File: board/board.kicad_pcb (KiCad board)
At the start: 2 copper layers, 91.3 x 53.3 mm, 87 parts, among them J1 USB_B_Micro, J4 SWD_CONN, J5 JTAG_CONN, J6 UART_Conn, J7 SPI_CONN, J8 I2C_CONN, SW1 SW_DP3T, SW2 SW_DP3T, SW3 SW_DPDT_x2, U1 FT2232H-56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

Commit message: Update for release.
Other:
- board text added: "Mode"
- board text added: "Rev 5 OSHW - Apache 2 (C) 2020 Google LLC Designed by @Matir"
- board text added: "Test Interface for Multiple Embedded Protocols (TIMEP)"
- board text removed: "Universal IoT Tool (UNIT) (C) 2019 Google LLC Designed by: David Tomaschik (@Matir) Rev 3"

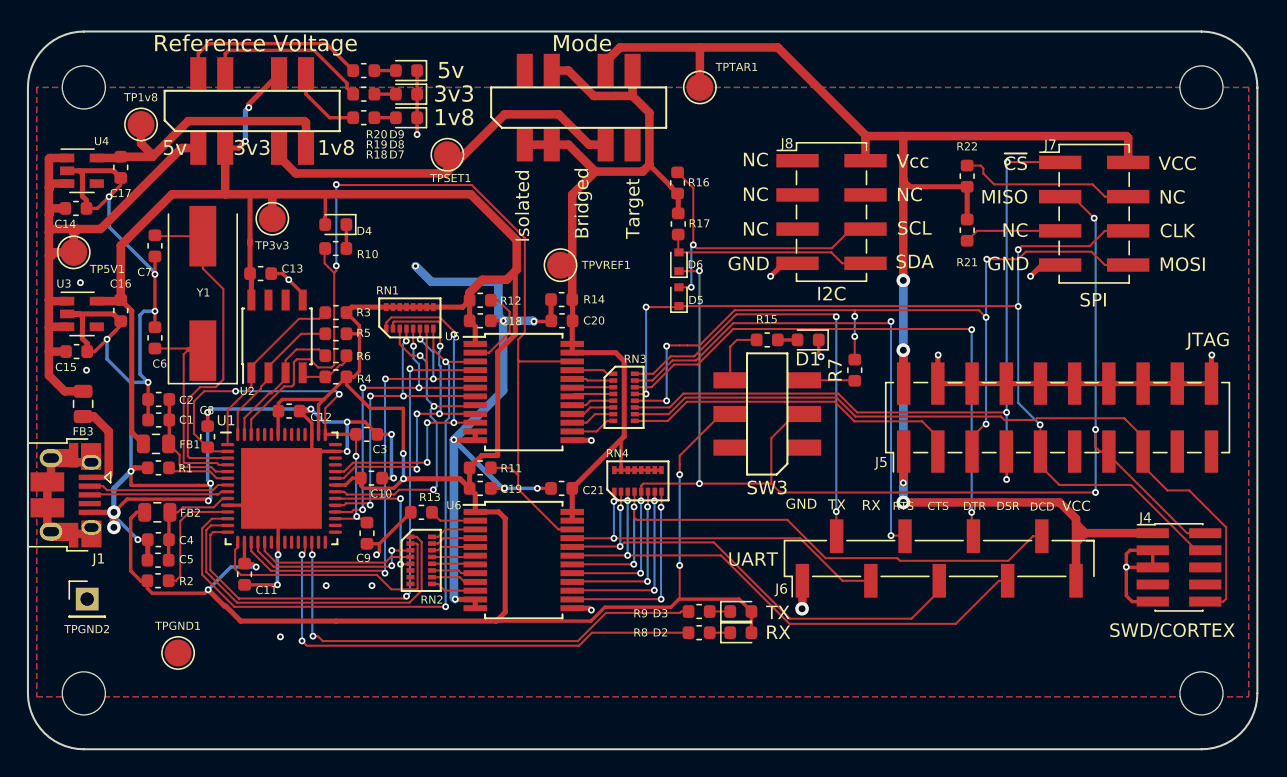
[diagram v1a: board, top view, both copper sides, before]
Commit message: Add protection (ESD, PTC fusing) to MicroUSB port
Schematic changes:

* No connect SHIELD on the MicroUSB port. Since we have no SHIELD GND, I
think it's best to leave the shield unconnected rather than connect it
to our digital GND and potentially introduce noise. This seems to be
backed up by the FTDI USB Design Guidelines
(https://www.ftdichip.com/Support/Documents/AppNotes/AN_146_USB_Hardware_Design_Guidelines_for_FTDI_ICs.pdf)
* Inline a USBLC-6 for transient voltage supression on our USB data lines
and VBUS
* Add a 500mA hold current PTC after the ferrite bead on VBUS. This PTC
should help protect the host computer if the board short circuits

Layout changes:

* Moves the passives (C2, C1, FB1, R1, FB2, C4, C5, R2) around the
MicroUSB port slightly outward to make room for the USBLC-6
* Place USBLC-6 close to the MicroUSB port
* Place PTC next to FB3

Component Selection:

* USBLC-6 is a popular choice for USB transient voltage supression. It's
very low capacitance so it shouldn't have an impact on data
integrity/speed. The SOT-666 package is common and compact, but still
easy enough to place by hand. It's also cheap at just $0.32 (100x)
* The Littelfuse NanoSMD fuse is rated for 13.2V and a 500mA hold
current. It trips at 1.1A with a fast 100ms time to trip. The 1206
footprint is compact and it's easy to place by hand. It's pretty cheap
at $0.32 (100x)
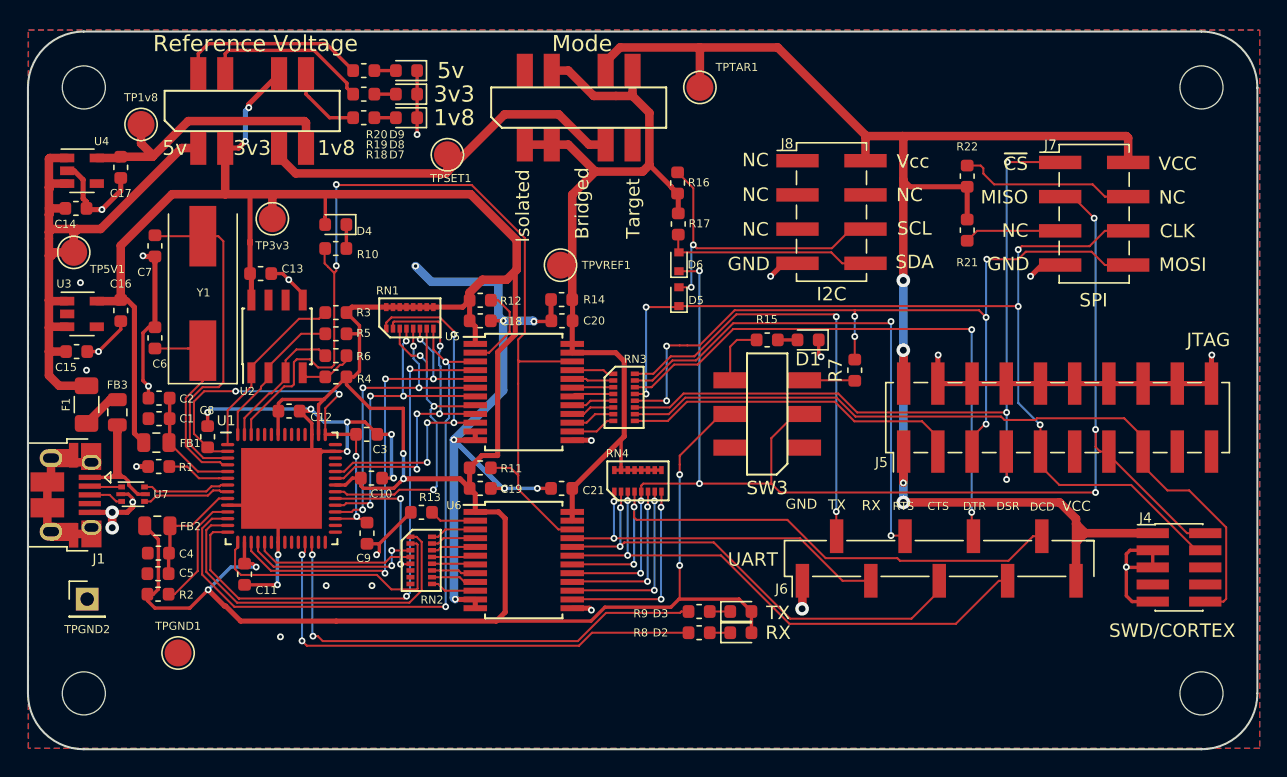
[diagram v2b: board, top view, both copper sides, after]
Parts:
- added F1: 500mA, Fuse:Fuse_1206_3216Metric, F.Cu at (92.2, 106.6)
- added U7: USBLC6, Package_TO_SOT_SMD:SOT-666, F.Cu at (95.7, 113.2)
- moved FB3 2.61 mm to (94.5, 107.1)
- moved C4 1.00 mm to (97.5, 117.6)
- moved C5 1.00 mm to (97.5, 119.1)
- moved FB2 1.00 mm to (97.5, 115.6)
- moved R2 1.00 mm to (97.5, 120.6)
- moved C1 0.10 mm to (97.6, 107.6)
- moved C2 0.10 mm to (97.6, 106.1)
- moved FB1 0.10 mm to (97.4, 109.4)
- moved R1 0.10 mm to (97.6, 111.2)
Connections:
- net Net-(FB3-Pad2) renamed /VBUS
- FB3 pad 1: +5V -> Net-(F1-Pad2)
- J1 pad 2: /USB_N -> Net-(J1-Pad2)
- J1 pad 3: /USB_P -> Net-(J1-Pad3)
- J1 pad 4: Net-(J1-Pad4) -> (no net)
- J1 pad 6: GND -> Net-(J1-Pad6)
- J4 pad 6: Net-(J4-Pad6) -> (no net)
- J4 pad 7: Net-(J4-Pad7) -> (no net)
- J4 pad 8: Net-(J4-Pad8) -> (no net)
- J5 pad 11: Net-(J5-Pad11) -> (no net)
- J5 pad 17: Net-(J5-Pad17) -> (no net)
- J5 pad 19: Net-(J5-Pad19) -> (no net)
- J8 pad 1: Net-(J8-Pad1) -> (no net)
- J8 pad 3: Net-(J8-Pad3) -> (no net)
- J8 pad 4: Net-(J8-Pad4) -> (no net)
- J8 pad 5: Net-(J8-Pad5) -> (no net)
- RN2 pad 6: Net-(RN2-Pad6) -> (no net)
- RN2 pad 7: Net-(RN2-Pad7) -> (no net)
- RN2 pad 8: Net-(RN2-Pad8) -> (no net)
- SW2 pad 4: Net-(SW2-Pad4) -> (no net)
- SW2 pad 5: Net-(SW2-Pad5) -> (no net)
- SW3 pad 1: Net-(SW3-Pad1) -> (no net)
- SW3 pad 4: Net-(SW3-Pad4) -> (no net)
- U1 pad 20: /FT2232 Module/ADBUS7 -> (no net)
- U1 pad 22: /FT2232 Module/ACBUS0 -> (no net)
- U1 pad 23: /FT2232 Module/ACBUS1 -> (no net)
- U1 pad 24: /FT2232 Module/ACBUS2 -> (no net)
- U1 pad 27: /FT2232 Module/ACBUS5 -> (no net)
- U1 pad 28: /FT2232 Module/ACBUS6 -> (no net)
- U1 pad 29: /FT2232 Module/ACBUS7 -> (no net)
- U1 pad 30: Net-(U1-Pad30) -> (no net)
- U1 pad 39: /FT2232 Module/BDBUS6 -> (no net)
- U1 pad 40: /FT2232 Module/BDBUS7 -> (no net)
- U1 pad 42: /FT2232 Module/BCBUS0 -> (no net)
- U1 pad 46: /FT2232 Module/BCBUS1 -> (no net)
- U1 pad 47: /FT2232 Module/BCBUS2 -> (no net)
- U1 pad 48: /FT2232 Module/BCBUS3 -> (no net)
- U1 pad 49: /FT2232 Module/BCBUS4 -> (no net)
- U1 pad 51: /FT2232 Module/BCBUS5 -> (no net)
- U1 pad 52: /FT2232 Module/BCBUS6 -> (no net)
- U1 pad 53: /FT2232 Module/BCBUS7 -> (no net)
- U2 pad 6: Net-(U2-Pad6) -> (no net)
- U2 pad 7: Net-(U2-Pad7) -> (no net)
- U3 pad 4: Net-(U3-Pad4) -> (no net)
- U4 pad 4: Net-(U4-Pad4) -> (no net)
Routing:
- net GND: track 266.7 -> 194.6 mm, vias 43 -> 40
- net Net-(J1-Pad6): track 0.00 -> 11.9 mm
- net /USB_N: track 10.5 -> 6.51 mm
- net /USB_P: track 10.4 -> 6.55 mm
- net Net-(F1-Pad2): track 0.00 -> 3.02 mm
- net Net-(J1-Pad3): track 0.00 -> 2.56 mm
- net /VBUS: track 7.06 -> 9.54 mm
- net Net-(J1-Pad2): track 0.00 -> 2.39 mm
- net /FT2232 Module/OSCO: track 16.9 -> 14.9 mm
